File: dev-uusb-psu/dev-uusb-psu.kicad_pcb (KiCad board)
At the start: 2 copper layers, 21.8 x 20.8 mm, 11 parts, among them J1 Conn_01x03_Male, J2 Conn_01x03_Male

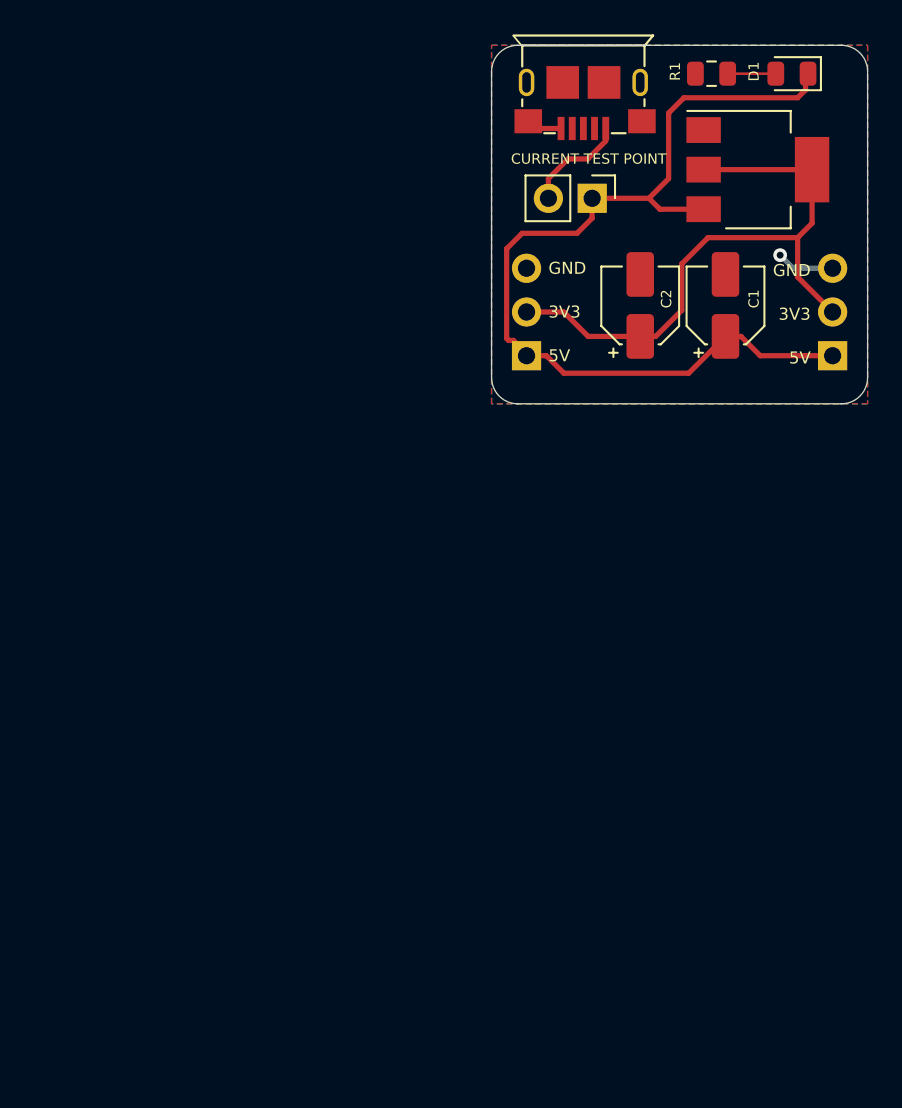
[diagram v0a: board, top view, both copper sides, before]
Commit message: Updated connectors
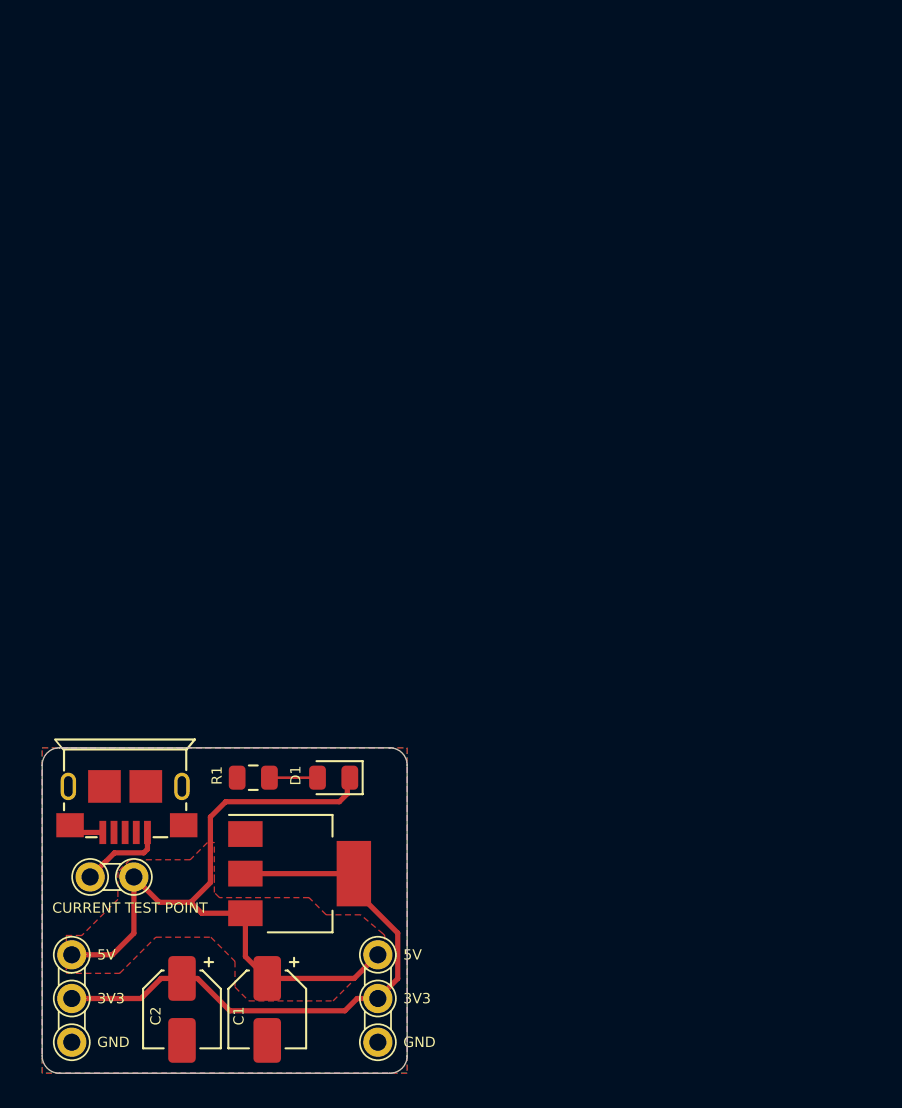
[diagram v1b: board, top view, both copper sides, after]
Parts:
- removed DEV-UUSB-PSU: LOGO_BRD_REF, qboards_aesthetics:logo_url-3mm
- removed TP_CURRENT1: Conn_01x02_Male, Connector_PinHeader_2.54mm:PinHeader_1x02_P2.54mm_Vertical
- removed [BRD_REF]: LOGO_BRD_REF, qboards_aesthetics:logo-10mm
- added CURRENT TEST POINT: Conn_01x02_Male, qboards_connectors:PinHeader_1x02_P2.54mm_Vertical, F.Cu at (112.8, 130.1)
- added REF**: breadboard-guide, qboards_aesthetics:breadboard-guide, F.Cu at (94.0, 121.9)
- J1, J2: footprint Connector_PinHeader_2.54mm:PinHeader_1x03_P2.54mm_Vertical -> qboards_connectors:PinHeader_1x03_P2.54mm_Vertical; moved to F.Cu
- moved D1 48.8 mm to (124.4, 124.3)
- moved VREG1 48.8 mm to (122.5, 129.9)
- moved R1 48.8 mm to (119.8, 124.3)
- moved C1 48.8 mm to (120.6, 137.8), turned to 270 degrees
- moved C2 48.8 mm to (115.6, 137.8), turned to 270 degrees
- moved USB1 48.8 mm to (112.3, 124.8)
- moved J1 43.7 mm to (109.2, 134.6)
- moved J2 43.7 mm to (127.0, 134.6)
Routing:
- net +5V: track 55.7 -> 40.8 mm
- net GND: track 5.44 -> 2.08 mm, vias 1 -> 0
- net +3V3: track 36.1 -> 34.4 mm
- net Net-(TP_CURRENT1-Pad2): track 6.10 -> 4.97 mm
- added copper zone on F.Cu, net +5V
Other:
- board size 21.8 x 20.8 mm -> 21.2 x 18.9 mm
- board text removed: "3V3"
- board text removed: "5V"
- board text removed: "CURRENT TEST POINT"
- board text removed: "GND"
